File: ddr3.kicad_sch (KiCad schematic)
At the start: 0 parts

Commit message: Completed schematic of MT41K128M16JT memory module
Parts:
- added C25, C26, C27, C28, C29, C30, C31, C32, C33, C34: C_100n_0402, antmicro-footprints:0402-cap, symbol antmicroCapacitors0402:C_100n_0402
- added R25: R_100R_0402, antmicro-footprints:0402-res, symbol antmicroResistors0402:R_100R_0402
- added R26, R27, R28, R29, R30, R31: 4x51R_0402_array, antmicro-footprints:R_Array_4x0402, symbol antmicroResistorNetworksArrays:4x51R_0402_array
- added R32: R_240R_1%_0402, antmicro-footprints:0402-res, symbol antmicroResistors0402:R_240R_1%_0402
- added R33, R34: R_1k_0402, antmicro-footprints:0402-res, symbol antmicroResistors0402:R_1k_0402
- added TP1: TP, antmicro-footprints:TP-R-1.5, symbol antmicroTestPoints:TP
- added U7: MT41K128M16JT-125_K, antmicro-footprints:BGA80P96C6X16_800X1400X110, symbol antmicroMemory:MT41K128M16JT-125_K
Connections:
- new net: C33.2, C34.1, R33.1, R34.2, TP1.1, U7.H1 (VREFDQ), U7.M8 (VREFCA)
- new net: R32.2, U7.L8 (ZQ)
- new net +1V35: C25.1, C26.1, C27.1, C28.1, C29.1, C30.1, C31.1, C32.1, C33.1, R33.2, U7.A1 (VDDQ), U7.A8 (VDDQ), U7.B2 (VDD), U7.C1 (VDDQ), U7.C9 (VDDQ), U7.D2 (VDDQ), U7.D9 (VDD), U7.E9 (VDDQ), U7.F1 (VDDQ), U7.G7 (VDD), U7.H2 (VDDQ), U7.H9 (VDDQ), U7.K2 (VDD), U7.K8 (VDD), U7.N1 (VDD), U7.N9 (VDD), U7.R1 (VDD), U7.R9 (VDD)
- new net DDR3_A0: R26.1, U7.N3 (A0)
- new net DDR3_A1: R26.2, U7.P7 (A1)
- new net DDR3_A10: R28.3, U7.L7 (A10/AP)
- new net DDR3_A11: R28.4, U7.R7 (A11)
- new net DDR3_A12: R29.1, U7.N7 (A12/!BC)
- new net DDR3_A13: R29.2, U7.T3 (A13)
- new net DDR3_A2: R26.3, U7.P3 (A2)
- new net DDR3_A3: R26.4, U7.N2 (A3)
- new net DDR3_A4: R27.1, U7.P8 (A4)
- new net DDR3_A5: R27.2, U7.P2 (A5)
- new net DDR3_A6: R27.3, U7.R8 (A6)
- new net DDR3_A7: R27.4, U7.R2 (A7)
- new net DDR3_A8: R28.1, U7.T8 (A8)
- new net DDR3_A9: R28.2, U7.R3 (A9)
- new net DDR3_BA0: R29.3, U7.M2 (BA0)
- new net DDR3_BA1: R29.4, U7.N8 (BA1)
- new net DDR3_BA2: R31.4, U7.M3 (BA2)
- new net DDR3_CK: R25.2, U7.J7 (CK)
- new net DDR3_CKE: R31.3, U7.K9 (CKE)
- new net DDR3_DQ0: U7.E3 (DQ0)
- new net DDR3_DQ1: U7.F7 (DQ1)
- new net DDR3_DQ10: U7.C8 (DQ10)
- new net DDR3_DQ11: U7.C2 (DQ11)
- new net DDR3_DQ12: U7.A7 (DQ12)
- new net DDR3_DQ13: U7.A2 (DQ13)
- new net DDR3_DQ14: U7.B8 (DQ14)
- new net DDR3_DQ15: U7.A3 (DQ15)
- new net DDR3_DQ2: U7.F2 (DQ2)
- new net DDR3_DQ3: U7.F8 (DQ3)
- new net DDR3_DQ4: U7.H3 (DQ4)
- new net DDR3_DQ5: U7.H8 (DQ5)
- new net DDR3_DQ6: U7.G2 (DQ6)
- new net DDR3_DQ7: U7.H7 (DQ7)
- new net DDR3_DQ8: U7.D7 (DQ8)
- new net DDR3_DQ9: U7.C3 (DQ9)
- new net DDR3_LDM: U7.E7 (LDM)
- new net DDR3_LDQS: U7.F3 (LDQS)
- new net DDR3_ODT: R31.2, U7.K1 (ODT)
- new net DDR3_UDM: U7.D3 (UDM)
- new net DDR3_UDQS: U7.C7 (UDQS)
- new net GND: C25.2, C26.2, C27.2, C28.2, C29.2, C30.2, C31.2, C32.2, C34.2, R32.1, R34.1, U7.A9 (VSS), U7.B1 (VSSQ), U7.B3 (VSS), U7.B9 (VSSQ), U7.D1 (VSSQ), U7.D8 (VSSQ), U7.E1 (VSS), U7.E2 (VSSQ), U7.E8 (VSSQ), U7.F9 (VSSQ), U7.G1 (VSSQ), U7.G8 (VSS), U7.G9 (VSSQ), U7.J2 (VSS), U7.J8 (VSS), U7.M1 (VSS), U7.M9 (VSS), U7.P1 (VSS), U7.P9 (VSS), U7.T1 (VSS), U7.T9 (VSS)
- new net Vtt: R26.5, R26.6, R26.7, R26.8, R27.5, R27.6, R27.7, R27.8, R28.5, R28.6, R28.7, R28.8, R29.5, R29.6, R29.7, R29.8, R30.5, R30.6, R30.7, R30.8, R31.5, R31.6, R31.7, R31.8
- new net ~{DDR3_CAS}: R30.3, U7.K3 (~{CAS})
- new net ~{DDR3_CK}: R25.1, U7.K7 (~{CK})
- new net ~{DDR3_CS}: R31.1, U7.L2 (~{CS})
- new net ~{DDR3_LDQS}: U7.G3 (~{LDQS})
- new net ~{DDR3_RAS}: R30.2, U7.J3 (~{RAS})
- new net ~{DDR3_RESET}: R30.1, U7.T2 (~{RESET})
- new net ~{DDR3_UDQS}: U7.B7 (~{UDQS})
- new net ~{DDR3_WE}: R30.4, U7.L3 (~{WE})
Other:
- note added: "MT41K128M16JT"
- note added: "Signal terminations can be rearanged for easier routing"

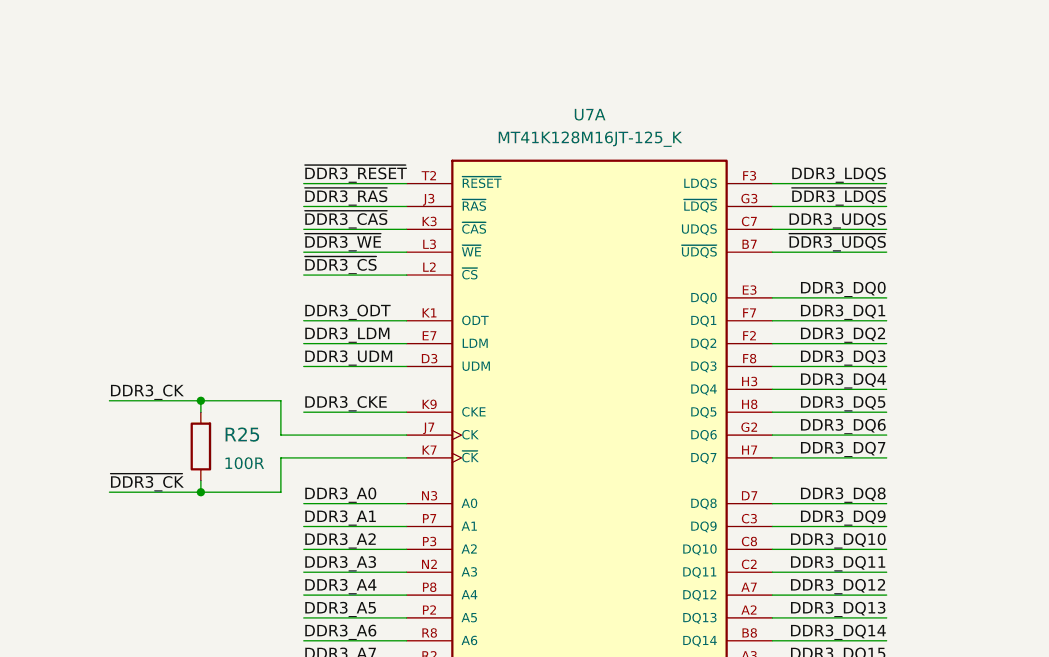
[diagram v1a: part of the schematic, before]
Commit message: Fixed differential pair names
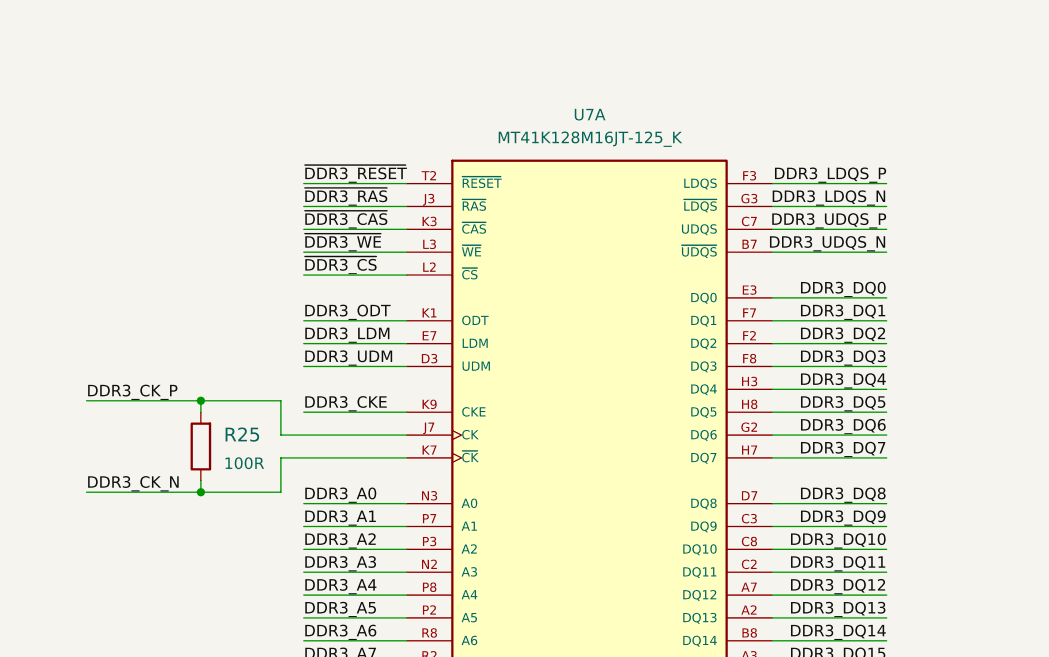
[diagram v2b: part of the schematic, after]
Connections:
- net DDR3_CK renamed DDR3_CK_P
- net DDR3_LDQS renamed DDR3_LDQS_P
- net DDR3_UDQS renamed DDR3_UDQS_P
- net ~{DDR3_CK} renamed DDR3_CK_N
- net ~{DDR3_LDQS} renamed DDR3_LDQS_N
- net ~{DDR3_UDQS} renamed DDR3_UDQS_N
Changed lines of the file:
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@@
     (stroke (width 0) (type default) (color 0 0 0 0))
   )
-  (wire (pts (xy 31.75 59.69) (xy 41.91 59.69))
+  (wire (pts (xy 29.21 59.69) (xy 41.91 59.69))
     (stroke (width 0) (type default) (color 0 0 0 0))
   )
@@
     (stroke (width 0) (type default) (color 0 0 0 0))
   )
-  (wire (pts (xy 31.75 69.85) (xy 41.91 69.85))
+  (wire (pts (xy 29.21 69.85) (xy 41.91 69.85))
     (stroke (width 0) (type default) (color 0 0 0 0))
   )
@@
     (effects (font (size 1.27 1.27)) (justify left bottom))
   )
-  (label "~{DDR3_UDQS}" (at 118.11 43.18 180)
+  (label "DDR3_UDQS_N" (at 118.11 43.18 180)
     (effects (font (size 1.27 1.27)) (justify right bottom))
   )
@@
     (effects (font (size 1.27 1.27)) (justify left bottom))
   )
-  (label "~{DDR3_CK}" (at 31.75 69.85 0)
+  (label "DDR3_CK_N" (at 29.21 69.85 0)
     (effects (font (size 1.27 1.27)) (justify left bottom))
   )
@@
     (effects (font (size 1.27 1.27)) (justify left bottom))
   )
-  (label "DDR3_LDQS" (at 118.11 35.56 180)
+  (label "DDR3_LDQS_P" (at 118.11 35.56 180)
     (effects (font (size 1.27 1.27)) (justify right bottom))
   )
@@
     (effects (font (size 1.27 1.27)) (justify right bottom))
   )
-  (label "DDR3_UDQS" (at 118.11 40.64 180)
-    (effects (font (size 1.27 1.27)) (justify right bottom))
-  )
-  (label "DDR3_CK" (at 31.75 59.69 0)
+  (label "DDR3_UDQS_P" (at 118.11 40.64 180)
+    (effects (font (size 1.27 1.27)) (justify right bottom))
+  )
+  (label "DDR3_CK_P" (at 29.21 59.69 0)
     (effects (font (size 1.27 1.27)) (justify left bottom))
   )
@@
     (effects (font (size 1.27 1.27)) (justify right bottom))
   )
-  (label "~{DDR3_LDQS}" (at 118.11 38.1 180)
-    (effects (font (size 1.27 1.27)) (justify right bottom))
-  )
+  (label "DDR3_LDQS_N" (at 118.11 38.1 180)
+    (effects (font (size 1.27 1.27)) (justify right bottom))
+  )

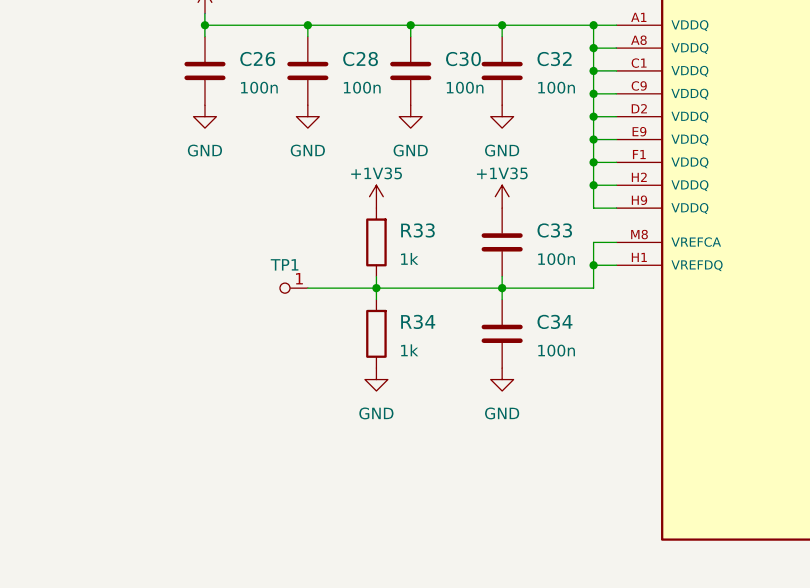
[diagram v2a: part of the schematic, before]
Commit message: Added DDR3 Vtt and Vref regulator
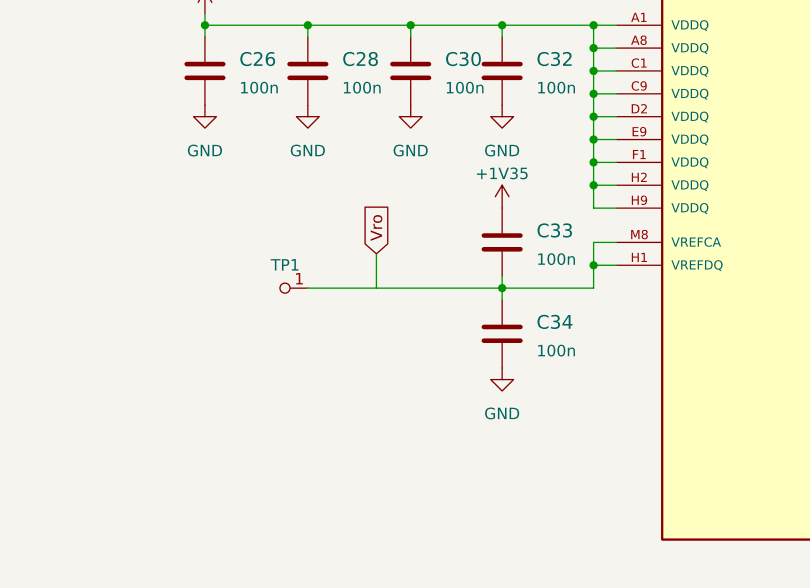
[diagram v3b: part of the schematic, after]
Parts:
- removed R33, R34: R_1k_0402, antmicro-footprints:0402-res, symbol antmicroResistors0402:R_1k_0402
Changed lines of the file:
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@@
   (junction (at 207.01 73.66) (diameter 0) (color 0 0 0 0)
   )
-  (junction (at 182.88 100.33) (diameter 0) (color 0 0 0 0)
-  )
   (wire (pts (xy 252.73 49.53) (xy 252.73 52.07))
     (stroke (width 0) (type default) (color 0 0 0 0))
@@
     (stroke (width 0) (type default) (color 0 0 0 0))
   )
-  (wire (pts (xy 175.26 100.33) (xy 182.88 100.33))
+  (wire (pts (xy 175.26 100.33) (xy 196.85 100.33))
     (stroke (width 0) (type default) (color 0 0 0 0))
   )
@@
     (stroke (width 0) (type default) (color 0 0 0 0))
   )
-  (wire (pts (xy 182.88 99.06) (xy 182.88 100.33))
+  (wire (pts (xy 182.88 96.52) (xy 182.88 100.33))
     (stroke (width 0) (type default) (color 0 0 0 0))
   )
@@
     (stroke (width 0) (type default) (color 0 0 0 0))
   )
-  (wire (pts (xy 182.88 100.33) (xy 182.88 101.6))
-    (stroke (width 0) (type default) (color 0 0 0 0))
-  )
   (wire (pts (xy 29.21 69.85) (xy 41.91 69.85))
     (stroke (width 0) (type default) (color 0 0 0 0))
@@
   )
   (wire (pts (xy 76.2 162.56) (xy 76.2 160.02))
-    (stroke (width 0) (type default) (color 0 0 0 0))
-  )
-  (wire (pts (xy 182.88 100.33) (xy 196.85 100.33))
     (stroke (width 0) (type default) (color 0 0 0 0))
   )
@@
     )
   )
+  (global_label "Vro" (shape input) (at 182.88 96.52 90) (fields_autoplaced)
+    (effects (font (size 1.27 1.27)) (justify left))
+    (property "Intersheet References" "${INTERSHEET_REFS}" (id 0) (at 182.8006 91.0831 90)
+      (effects (font (size 1.27 1.27)) (justify left) hide)
+    )
+  )
   (global_label "Vtt" (shape input) (at 110.49 129.54 90) (fields_autoplaced)
     (effects (font (size 1.27 1.27)) (justify left))
@@
     )
     (pin "1")
-  )
-  (symbol (lib_id "antmicroResistors0402:R_1k_0402") (at 182.88 95.25 90) (unit 1)
-    (in_bom yes) (on_board yes) (fields_autoplaced)
-    (property "Reference" "R33" (id 0) (at 185.42 93.98 90)
-      (effects (font (size 1.524 1.524)) (justify right))
-    )
-    (property "Value" "R_1k_0402" (id 1) (at 186.69 95.25 0)
-      (effects (font (size 1.524 1.524)) hide)
-    )
-    (property "Footprint" "antmicro-footprints:0402-res" (id 2) (at 177.8 90.17 0)
-      (effects (font (size 1.524 1.524)) (justify left) hide)
-    )
-    (property "Datasheet" "" (id 3) (at 182.88 95.25 0)
-      (effects (font (size 1.27 1.27)) hide)
-    )
-    (property "Manufacturer" "BOURNS" (id 4) (at 172.72 90.17 0)
-      (effects (font (size 1.524 1.524)) (justify left) hide)
-    )
-    (property "MPN" "CR0402-FX-1001GLF" (id 5) (at 175.26 90.17 0)
-      (effects (font (size 1.524 1.524)) (justify left) hide)
-    )
-    (property "Val" "1k" (id 6) (at 185.42 97.1549 90)
-      (effects (font (size 1.27 1.27)) (justify right))
-    )
-    (pin "1")
-    (pin "2")
   )
   (symbol (lib_id "power:GND") (at 175.26 55.88 0) (unit 1)
@@
     (pin "1")
   )
-  (symbol (lib_id "power:GND") (at 182.88 109.22 0) (unit 1)
-    (in_bom yes) (on_board yes) (fields_autoplaced)
-    (property "Reference" "#PWR0158" (id 0) (at 182.88 115.57 0)
-      (effects (font (size 1.27 1.27)) hide)
-    )
-    (property "Value" "GND" (id 1) (at 182.88 114.3 0))
-    (property "Footprint" "" (id 2) (at 182.88 109.22 0)
-      (effects (font (size 1.27 1.27)) hide)
-    )
-    (property "Datasheet" "" (id 3) (at 182.88 109.22 0)
-      (effects (font (size 1.27 1.27)) hide)
-    )
-    (pin "1")
-  )
-  (symbol (lib_id "power:+1V35") (at 182.88 91.44 0) (unit 1)
-    (in_bom yes) (on_board yes)
-    (property "Reference" "#PWR0159" (id 0) (at 182.88 95.25 0)
-      (effects (font (size 1.27 1.27)) hide)
-    )
-    (property "Value" "+1V35" (id 1) (at 182.88 87.63 0))
-    (property "Footprint" "" (id 2) (at 182.88 91.44 0)
-      (effects (font (size 1.27 1.27)) hide)
-    )
-    (property "Datasheet" "" (id 3) (at 182.88 91.44 0)
-      (effects (font (size 1.27 1.27)) hide)
-    )
-    (pin "1")
-  )
   (symbol (lib_id "antmicroCapacitors0402:C_100n_0402") (at 175.26 76.2 0) (unit 1)
     (in_bom yes) (on_board yes) (fields_autoplaced)
@@
     )
     (pin "1")
-    (pin "2")
-  )
-  (symbol (lib_id "antmicroResistors0402:R_1k_0402") (at 182.88 105.41 90) (unit 1)
-    (in_bom yes) (on_board yes) (fields_autoplaced)
-    (property "Reference" "R34" (id 0) (at 185.42 104.14 90)
-      (effects (font (size 1.524 1.524)) (justify right))
-    )
-    (property "Value" "R_1k_0402" (id 1) (at 186.69 105.41 0)
-      (effects (font (size 1.524 1.524)) hide)
-    )
-    (property "Footprint" "antmicro-footprints:0402-res" (id 2) (at 177.8 100.33 0)
-      (effects (font (size 1.524 1.524)) (justify left) hide)
-    )
-    (property "Datasheet" "" (id 3) (at 182.88 105.41 0)
-      (effects (font (size 1.27 1.27)) hide)
-    )
-    (property "Manufacturer" "BOURNS" (id 4) (at 172.72 100.33 0)
-      (effects (font (size 1.524 1.524)) (justify left) hide)
-    )
-    (property "MPN" "CR0402-FX-1001GLF" (id 5) (at 175.26 100.33 0)
-      (effects (font (size 1.524 1.524)) (justify left) hide)
-    )
-    (property "Val" "1k" (id 6) (at 185.42 107.3149 90)
-      (effects (font (size 1.27 1.27)) (justify right))
-    )
-    (pin "1")

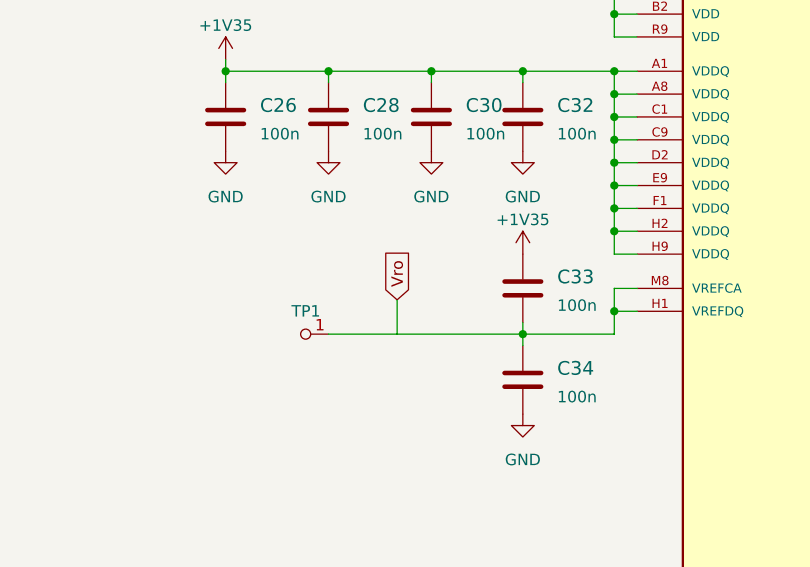
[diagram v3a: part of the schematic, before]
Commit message: Fixed VREF connection
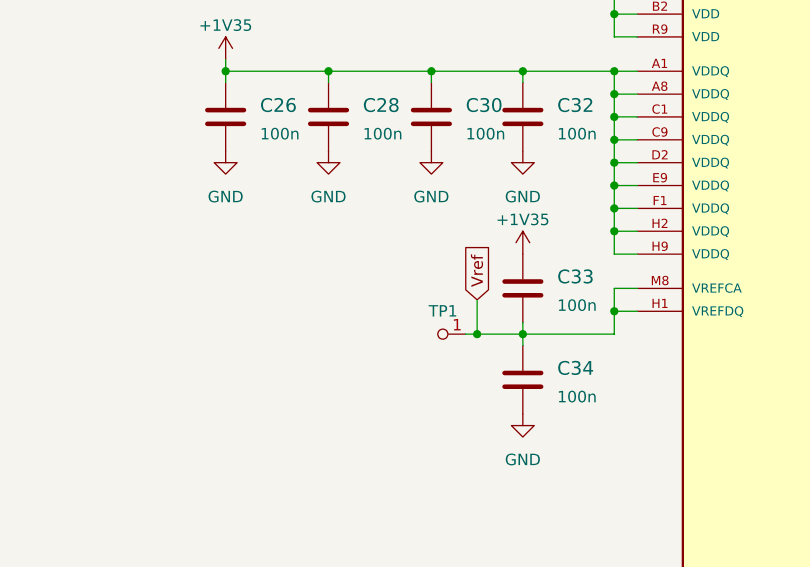
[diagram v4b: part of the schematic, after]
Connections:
- net Vref: now reaches C33.2, C34.1, TP1.1, U7.H1 (VREFDQ), U7.M8 (VREFCA)
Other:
- moved on the sheet: TP1
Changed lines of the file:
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@@
   (junction (at 163.83 46.99) (diameter 0) (color 0 0 0 0)
   )
+  (junction (at 191.77 100.33) (diameter 0) (color 0 0 0 0)
+  )
   (junction (at 76.2 160.02) (diameter 0) (color 0 0 0 0)
   )
@@
     (stroke (width 0) (type default) (color 0 0 0 0))
   )
-  (wire (pts (xy 175.26 100.33) (xy 196.85 100.33))
+  (wire (pts (xy 190.5 100.33) (xy 191.77 100.33))
     (stroke (width 0) (type default) (color 0 0 0 0))
   )
@@
     (stroke (width 0) (type default) (color 0 0 0 0))
   )
-  (wire (pts (xy 182.88 96.52) (xy 182.88 100.33))
-    (stroke (width 0) (type default) (color 0 0 0 0))
-  )
   (wire (pts (xy 209.55 95.25) (xy 207.01 95.25))
     (stroke (width 0) (type default) (color 0 0 0 0))
@@
     (stroke (width 0) (type default) (color 0 0 0 0))
   )
+  (wire (pts (xy 191.77 100.33) (xy 196.85 100.33))
+    (stroke (width 0) (type default) (color 0 0 0 0))
+  )
   (wire (pts (xy 68.58 176.53) (xy 76.2 176.53))
     (stroke (width 0) (type default) (color 0 0 0 0))
@@
   )
   (wire (pts (xy 110.49 151.13) (xy 110.49 154.94))
+    (stroke (width 0) (type default) (color 0 0 0 0))
+  )
+  (wire (pts (xy 191.77 96.52) (xy 191.77 100.33))
     (stroke (width 0) (type default) (color 0 0 0 0))
   )
@@
     )
   )
-  (global_label "Vro" (shape input) (at 182.88 96.52 90) (fields_autoplaced)
+  (global_label "Vref" (shape input) (at 191.77 96.52 90) (fields_autoplaced)
     (effects (font (size 1.27 1.27)) (justify left))
-    (property "Intersheet References" "${INTERSHEET_REFS}" (id 0) (at 182.8006 91.0831 90)
+    (property "Intersheet References" "${INTERSHEET_REFS}" (id 0) (at 191.6906 90.4179 90)
       (effects (font (size 1.27 1.27)) (justify left) hide)
     )
@@
     (pin "1")
   )
-  (symbol (lib_id "antmicroTestPoints:TP") (at 172.72 100.33 270) (unit 1)
-    (in_bom yes) (on_board yes) (fields_autoplaced)
-    (property "Reference" "TP1" (id 0) (at 172.7581 97.79 90))
-    (property "Value" "TP" (id 1) (at 172.72 100.33 0)
-      (effects (font (size 1.27 1.27)) hide)
-    )
-    (property "Footprint" "antmicro-footprints:TP-R-1.5" (id 2) (at 172.72 100.33 0)
-      (effects (font (size 1.27 1.27)) hide)
-    )
-    (property "Datasheet" "" (id 3) (at 172.72 100.33 0)
-      (effects (font (size 1.27 1.27)) hide)
-    )
+  (symbol (lib_id "antmicroTestPoints:TP") (at 187.96 100.33 270) (unit 1)
+    (in_bom yes) (on_board yes) (fields_autoplaced)
+    (property "Reference" "TP1" (id 0) (at 187.9981 97.79 90))
+    (property "Value" "TP" (id 1) (at 187.96 100.33 0)
+      (effects (font (size 1.27 1.27)) hide)
+    )
+    (property "Footprint" "antmicro-footprints:TP-R-1.5" (id 2) (at 187.96 100.33 0)
+      (effects (font (size 1.27 1.27)) hide)
+    )
+    (property "Datasheet" "" (id 3) (at 187.96 100.33 0)
+      (effects (font (size 1.27 1.27)) hide)
+    )
